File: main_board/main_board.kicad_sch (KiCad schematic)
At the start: 4 parts

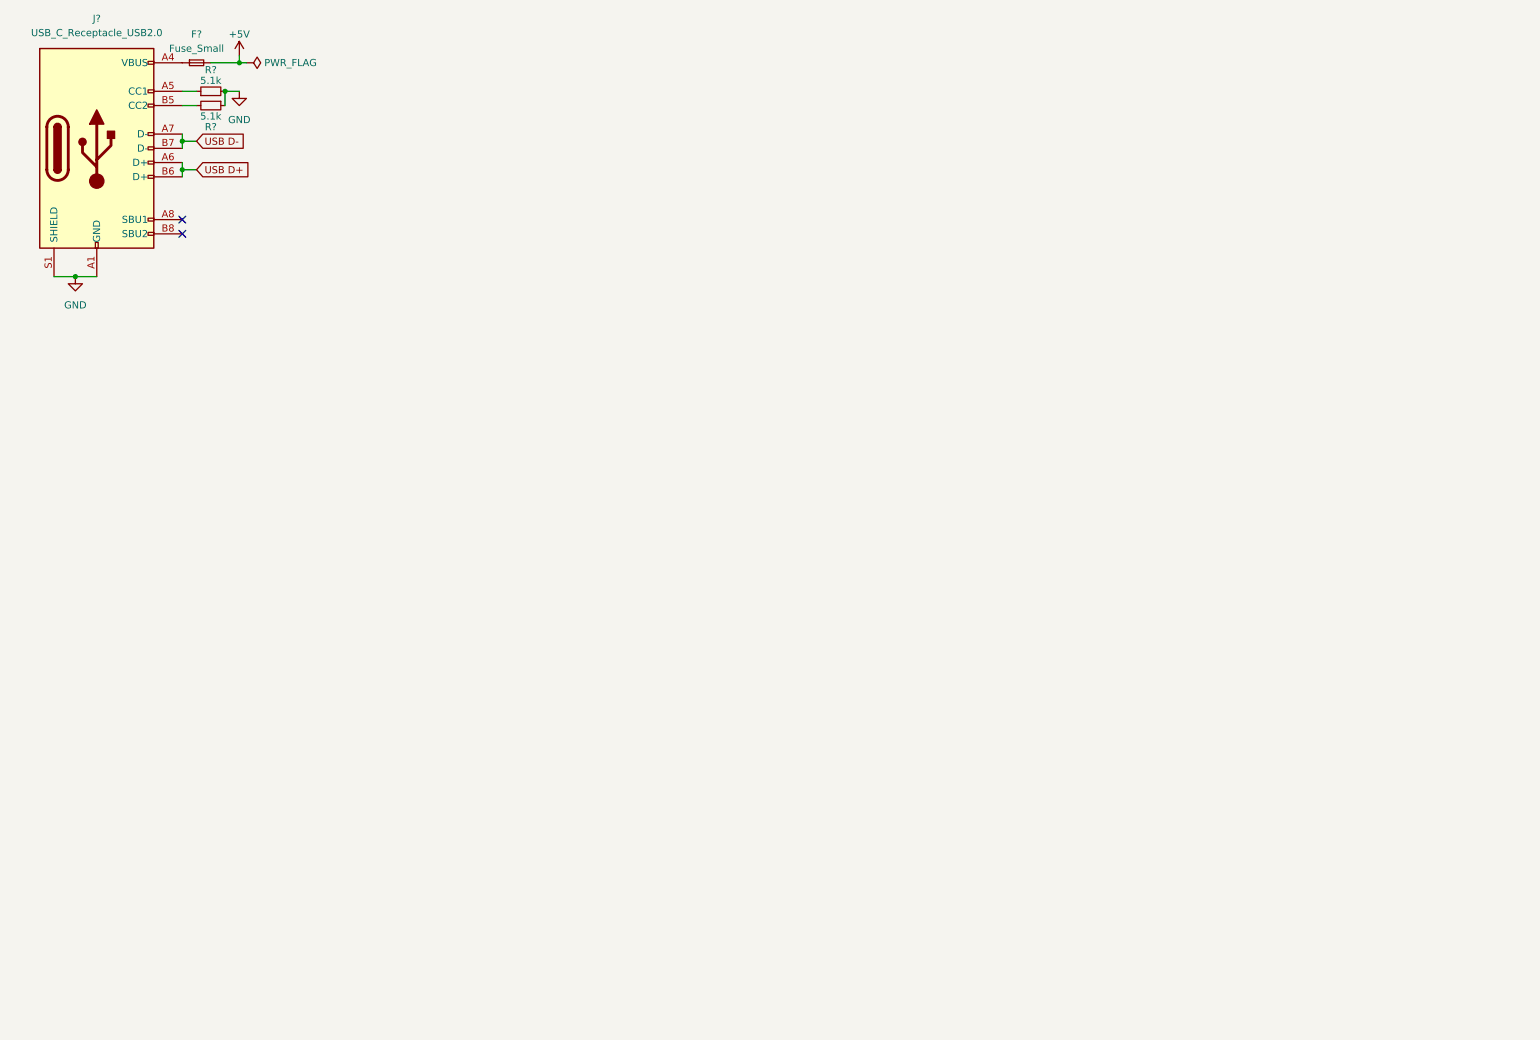
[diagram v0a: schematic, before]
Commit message: Main board schematic updates
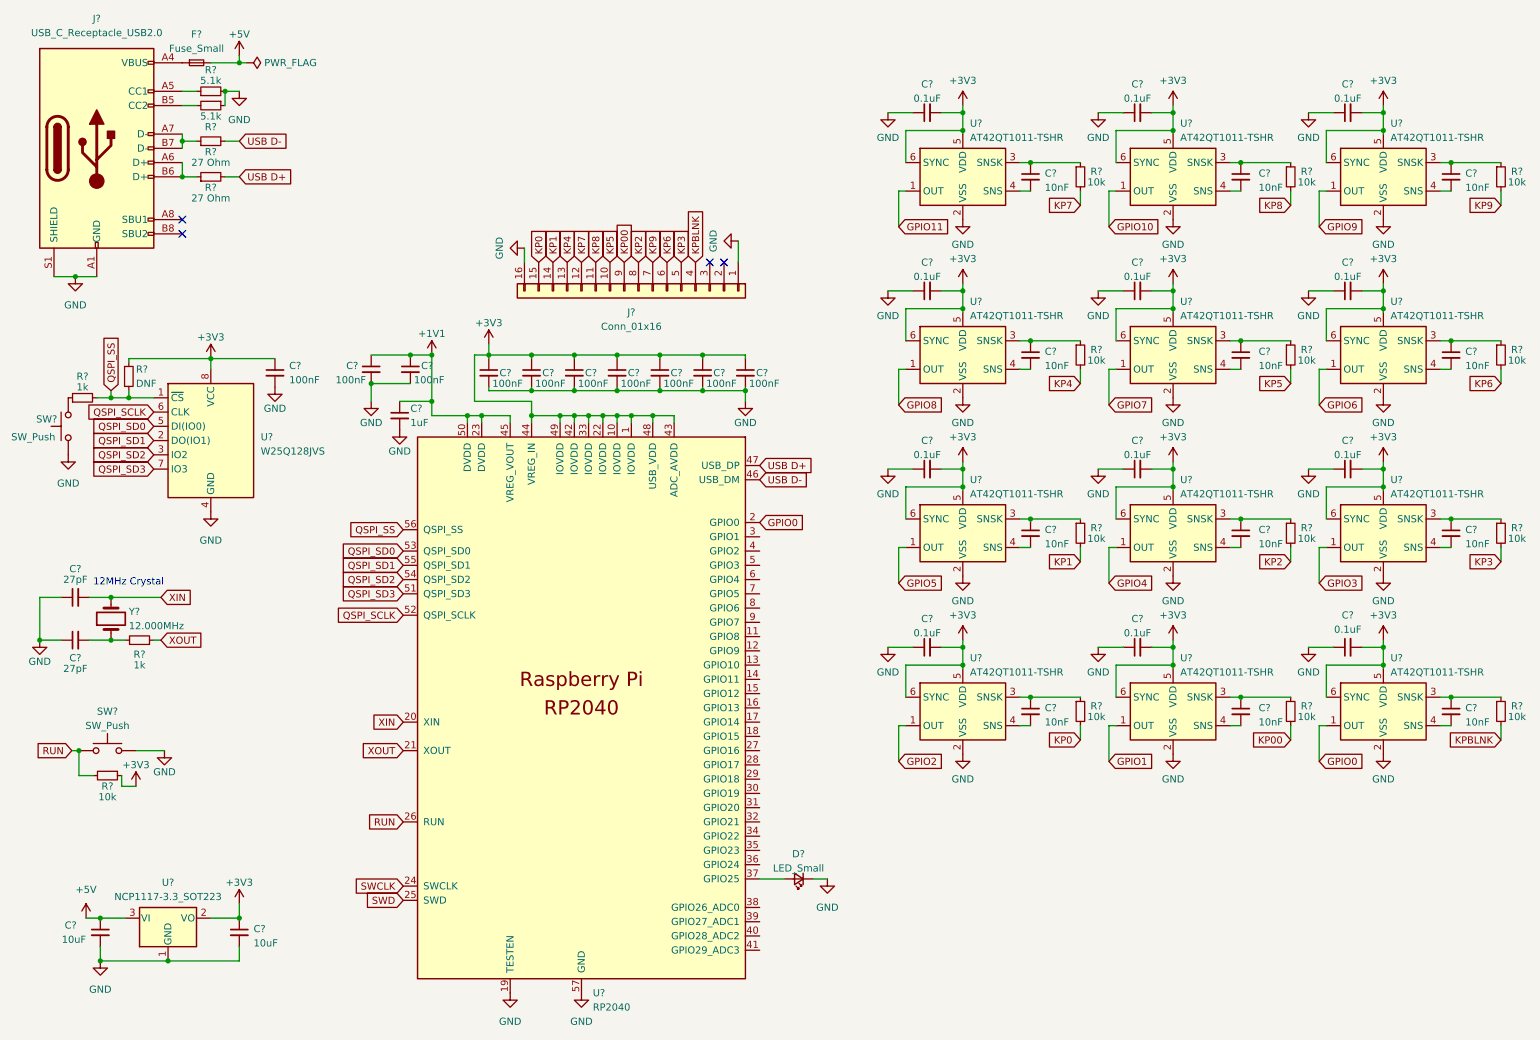
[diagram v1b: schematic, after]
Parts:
- added C? (x12): 0.1uF, symbol Device:C_Small
- added C? (x9): 100nF, symbol Device:C_Small
- added C? (x12): 10nF, symbol Device:C_Small
- added C?: 1uF, symbol Device:C_Small
- added C? (x2): 27pF, Capacitor_SMD:C_0402_1005Metric_Pad0.74x0.62mm_HandSolder, symbol Device:C_Small
- added C?: 100nF, Capacitor_SMD:C_0402_1005Metric_Pad0.74x0.62mm_HandSolder, symbol Device:C_Small
- added C? (x2): 10uF, Capacitor_SMD:C_0402_1005Metric_Pad0.74x0.62mm_HandSolder, symbol Device:C_Small
- added D?: LED_Small, LED_SMD:LED_0805_2012Metric_Pad1.15x1.40mm_HandSolder, symbol Device:LED_Small
- added J?: Conn_01x16, symbol Connector_Generic:Conn_01x16
- added R?: DNF, Resistor_SMD:R_0402_1005Metric_Pad0.72x0.64mm_HandSolder, symbol Device:R_Small
- added R? (x12): 10k, symbol Device:R_Small
- added R? (x2): 27 Ohm, symbol Device:R_Small
- added R? (x2): 1k, Resistor_SMD:R_0402_1005Metric_Pad0.72x0.64mm_HandSolder, symbol Device:R_Small
- added R?: 10k, Resistor_SMD:R_0402_1005Metric_Pad0.72x0.64mm_HandSolder, symbol Device:R_Small
- added SW?: SW_Push, Button_Switch_THT:SW_PUSH_6mm, symbol Switch:SW_Push
- added SW?: SW_Push, symbol Switch:SW_Push
- added U? (x12): AT42QT1011-TSHR, Package_TO_SOT_SMD:SOT-23-6, symbol Sensor_Touch:AT42QT1011-TSHR
- added U?: RP2040, RP2040_minimal:RP2040-QFN-56, symbol MCU_RaspberryPi_RP2040:RP2040
- added U?: W25Q128JVS, Package_SO:SOIC-8_5.23x5.23mm_P1.27mm, symbol Memory_Flash:W25Q128JVS
- added U?: NCP1117-3.3_SOT223, Package_TO_SOT_SMD:SOT-223-3_TabPin2, symbol Regulator_Linear:NCP1117-3.3_SOT223
- added Y?: 12.000MHz, Crystal:Crystal_HC49-4H_Vertical, symbol Device:Crystal
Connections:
- net +5V: now also C?.1, U?.3 (VI)
- net GND: now also C?.1, C?.1, C?.1, C?.1, C?.1, C?.1, C?.1, C?.1, C?.1, C?.1, C?.1, C?.1, C?.1, C?.1, C?.2, C?.2, C?.2, C?.2, C?.2, C?.2, C?.2, C?.2, C?.2, C?.2, C?.2, C?.2, C?.2, D?.1 (K), J?.1 (Pin_1), J?.16 (Pin_16), SW?.1, SW?.2, U?.1 (GND), U?.19 (TESTEN), U?.2 (VSS), U?.2 (VSS), U?.2 (VSS), U?.2 (VSS), U?.2 (VSS), U?.2 (VSS), U?.2 (VSS), U?.2 (VSS), U?.2 (VSS), U?.2 (VSS), U?.2 (VSS), U?.2 (VSS), U?.4 (GND), U?.57 (GND)
- net USB D+: now also R?.2, U?.47 (USB_DP); no longer J?.A6 (D+), J?.B6 (D+)
- net USB D-: now also R?.2, U?.46 (USB_DM); no longer J?.A7 (D-), J?.B7 (D-)
- new net: C?.1, R?.1, U?.3 (SNSK) (x12)
- new net: C?.2, U?.4 (SNS) (x12)
- new net: J?.A7 (D-), J?.B7 (D-), R?.1
- new net: D?.2 (A), U?.37 (GPIO25)
- new net: J?.A6 (D+), J?.B6 (D+), R?.1
- new net: C?.2, R?.1, Y?.1
- new net: R?.1, SW?.2
- new net +1V1: C?.1, C?.1, C?.1, U?.23 (DVDD), U?.45 (VREG_VOUT), U?.50 (DVDD)
- new net +3V3: C?.1, C?.1, C?.1, C?.1, C?.1, C?.1, C?.1, C?.1, C?.1, C?.2, C?.2, C?.2, C?.2, C?.2, C?.2, C?.2, C?.2, C?.2, C?.2, C?.2, C?.2, R?.1, R?.1, U?.1 (IOVDD), U?.10 (IOVDD), U?.2 (VO), U?.22 (IOVDD), U?.33 (IOVDD), U?.42 (IOVDD), U?.43 (ADC_AVDD), U?.44 (VREG_IN), U?.48 (USB_VDD), U?.49 (IOVDD), U?.5 (VDD), U?.5 (VDD), U?.5 (VDD), U?.5 (VDD), U?.5 (VDD), U?.5 (VDD), U?.5 (VDD), U?.5 (VDD), U?.5 (VDD), U?.5 (VDD), U?.5 (VDD), U?.5 (VDD), U?.6 (SYNC), U?.6 (SYNC), U?.6 (SYNC), U?.6 (SYNC), U?.6 (SYNC), U?.6 (SYNC), U?.6 (SYNC), U?.6 (SYNC), U?.6 (SYNC), U?.6 (SYNC), U?.6 (SYNC), U?.6 (SYNC), U?.8 (VCC)
- new net GPIO0: U?.1 (OUT), U?.2 (GPIO0)
- new net GPIO1: U?.1 (OUT)
- new net GPIO10: U?.1 (OUT)
- new net GPIO11: U?.1 (OUT)
- new net GPIO2: U?.1 (OUT)
- new net GPIO3: U?.1 (OUT)
- new net GPIO4: U?.1 (OUT)
- new net GPIO5: U?.1 (OUT)
- new net GPIO6: U?.1 (OUT)
- new net GPIO7: U?.1 (OUT)
- new net GPIO8: U?.1 (OUT)
- new net GPIO9: U?.1 (OUT)
- new net KP0: J?.15 (Pin_15), R?.2
- new net KP00: J?.9 (Pin_9), R?.2
- new net KP1: J?.14 (Pin_14), R?.2
- new net KP2: J?.8 (Pin_8), R?.2
- new net KP3: J?.5 (Pin_5), R?.2
- new net KP4: J?.13 (Pin_13), R?.2
- new net KP5: J?.10 (Pin_10), R?.2
- new net KP6: J?.6 (Pin_6), R?.2
- new net KP7: J?.12 (Pin_12), R?.2
- new net KP8: J?.11 (Pin_11), R?.2
- new net KP9: J?.7 (Pin_7), R?.2
- new net KPBLNK: J?.4 (Pin_4), R?.2
- new net QSPI_SCLK: U?.52 (QSPI_SCLK), U?.6 (CLK)
- new net QSPI_SD0: U?.5 (DI(IO0)), U?.53 (QSPI_SD0)
- new net QSPI_SD1: U?.2 (DO(IO1)), U?.55 (QSPI_SD1)
- new net QSPI_SD2: U?.3 (IO2), U?.54 (QSPI_SD2)
- new net QSPI_SD3: U?.51 (QSPI_SD3), U?.7 (IO3)
- new net QSPI_SS: R?.2, R?.2, U?.1 (~{CS}), U?.56 (QSPI_SS)
- new net RUN: R?.2, SW?.1, U?.26 (RUN)
- new net SWCLK: U?.24 (SWCLK)
- new net SWD: U?.25 (SWD)
- new net XIN: C?.2, U?.20 (XIN), Y?.2
- new net XOUT: R?.2, U?.21 (XOUT)
- no-connect marks 2 -> 4
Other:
- note added: "12MHz Crystal"

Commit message: done RP2040 routing, near final component layout
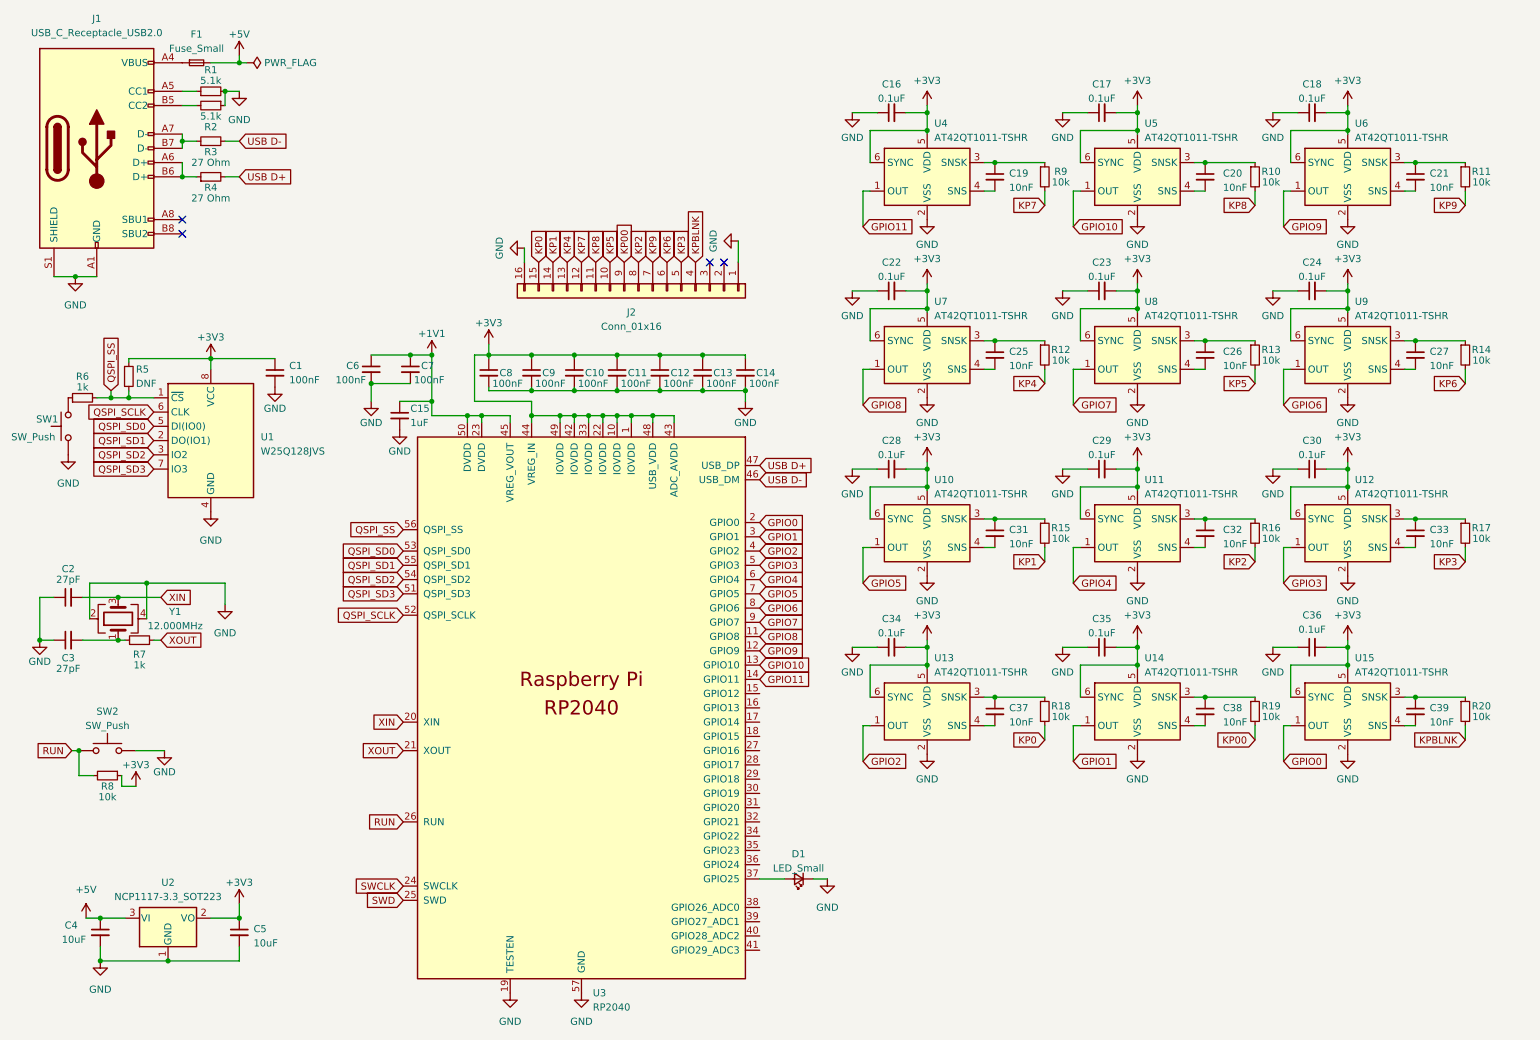
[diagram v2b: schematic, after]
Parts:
- removed Y?: 12.000MHz, Crystal:Crystal_HC49-4H_Vertical, symbol Device:Crystal
- added Y1: 12.000MHz, Crystal:Crystal_SMD_3225-4Pin_3.2x2.5mm_HandSoldering, symbol Device:Crystal_GND24
- C10, C11, C12, C13, C14, C15, C16, C17, C18, C19, C20, C21, C22, C23, C24, C25, C26, C27, C28, C29, C30, C31, C32, C33, C34, C35, C36, C37, C38, C39, C6, C7, C8, C9: renamed from C?; footprint (none) -> Capacitor_SMD:C_0603_1608Metric_Pad1.08x0.95mm_HandSolder
- F1: renamed from F?; footprint (none) -> Fuse:Fuse_1206_3216Metric_Pad1.42x1.75mm_HandSolder
- J1: renamed from J?; footprint (none) -> Connector_USB:USB_C_Receptacle_JAE_DX07S016JA1R1500
- J2: renamed from J?; footprint (none) -> Connector_FFC-FPC:TE_1-84952-6_1x16-1MP_P1.0mm_Horizontal
- R1, R10, R11, R12, R13, R14, R15, R16, R17, R18, R19, R2, R20, R3, R4, R9: renamed from R?; footprint (none) -> Resistor_SMD:R_0603_1608Metric_Pad0.98x0.95mm_HandSolder
- SW1: renamed from SW?; footprint (none) -> Button_Switch_THT:SW_PUSH_6mm
- gave numbers to parts that had none: 26
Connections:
- net GND: now also Y1.2, Y1.4
- net GPIO1: now also U3.3 (GPIO1)
- net GPIO10: now also U3.13 (GPIO10)
- net GPIO11: now also U3.14 (GPIO11)
- net GPIO2: now also U3.4 (GPIO2)
- net GPIO3: now also U3.5 (GPIO3)
- net GPIO4: now also U3.6 (GPIO4)
- net GPIO5: now also U3.7 (GPIO5)
- net GPIO6: now also U3.8 (GPIO6)
- net GPIO7: now also U3.9 (GPIO7)
- net GPIO8: now also U3.11 (GPIO8)
- net GPIO9: now also U3.12 (GPIO9)
- net XIN: now also Y1.3
- net at C3.2, R7.1: now also Y1.1
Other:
- note removed: "12MHz Crystal"
- moved on the sheet: C16, C17, C18, C19, C2, C20, C21, C22, C23, C24, C25, C26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

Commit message: move to MPR121
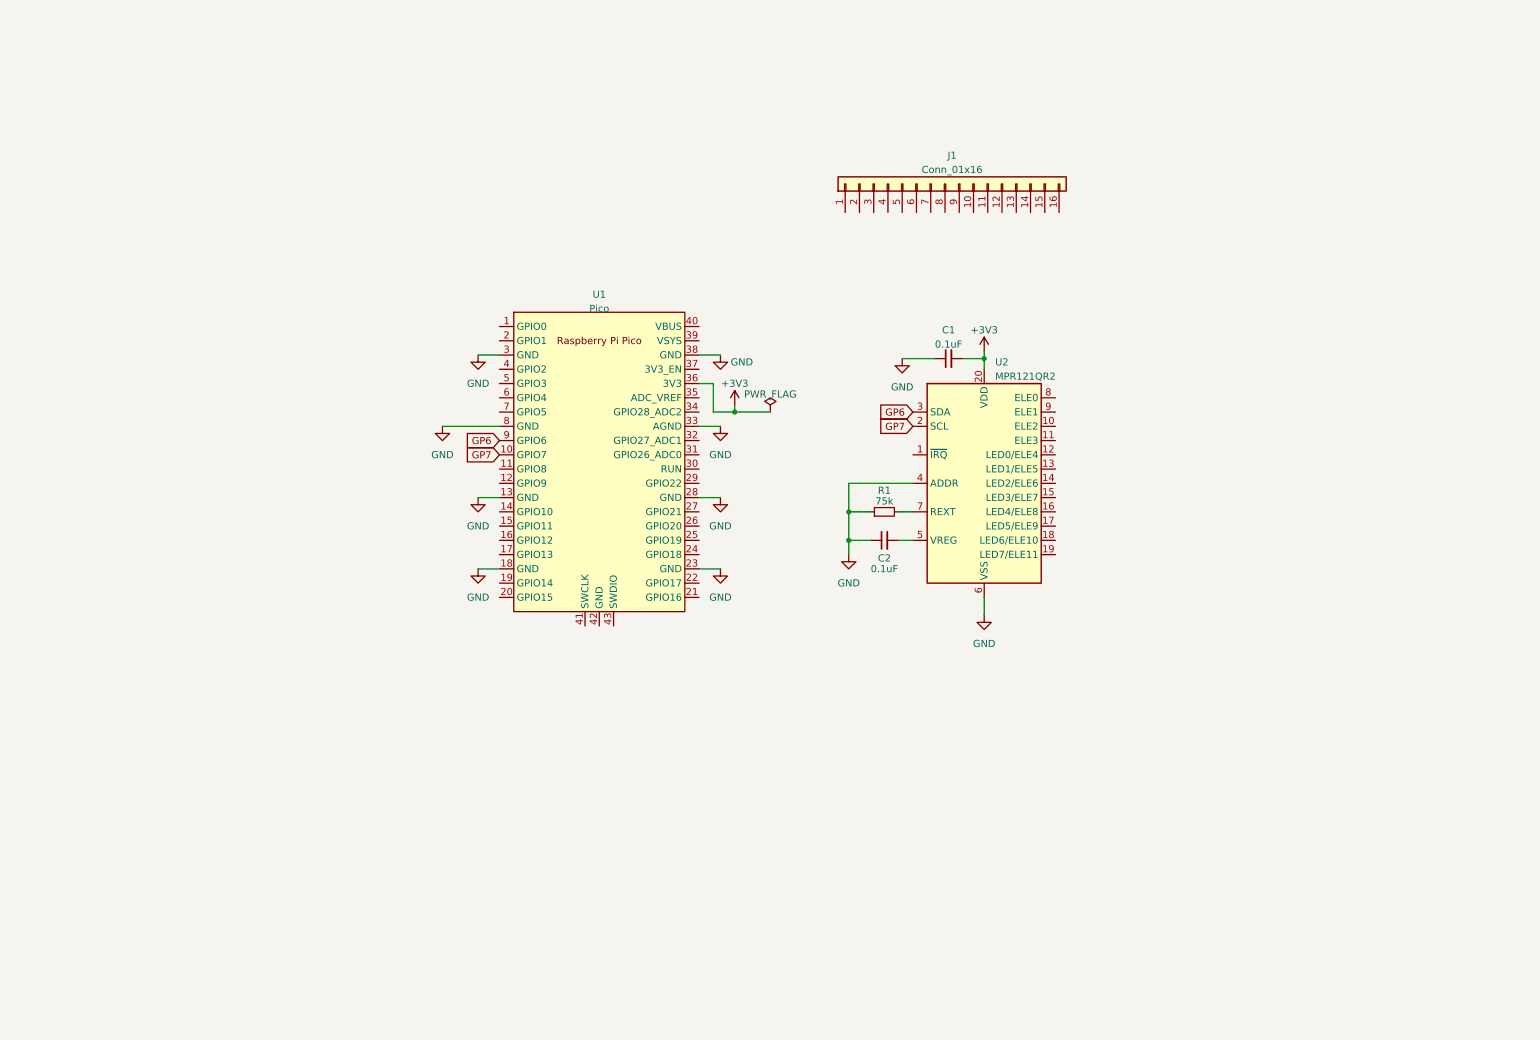
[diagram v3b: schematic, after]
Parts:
- removed C10, C11, C12, C13, C14, C6, C7, C8, C9: 100nF, Capacitor_SMD:C_0603_1608Metric_Pad1.08x0.95mm_HandSolder, symbol Device:C_Small
- removed C15: 1uF, Capacitor_SMD:C_0603_1608Metric_Pad1.08x0.95mm_HandSolder, symbol Device:C_Small
- removed C16, C17, C18, C22, C23, C24, C28, C29, C30, C34, C35, C36: 0.1uF, Capacitor_SMD:C_0603_1608Metric_Pad1.08x0.95mm_HandSolder, symbol Device:C_Small
- removed C19, C20, C21, C25, C26, C27, C31, C32, C33, C37, C38, C39: 10nF, Capacitor_SMD:C_0603_1608Metric_Pad1.08x0.95mm_HandSolder, symbol Device:C_Small
- removed C3: 27pF, Capacitor_SMD:C_0402_1005Metric_Pad0.74x0.62mm_HandSolder, symbol Device:C_Small
- removed C4, C5: 10uF, Capacitor_SMD:C_0402_1005Metric_Pad0.74x0.62mm_HandSolder, symbol Device:C_Small
- removed D1: LED_Small, LED_SMD:LED_0805_2012Metric_Pad1.15x1.40mm_HandSolder, symbol Device:LED_Small
- removed F1: Fuse_Small, Fuse:Fuse_1206_3216Metric_Pad1.42x1.75mm_HandSolder, symbol Device:Fuse_Small
- removed J1: USB_C_Receptacle_USB2.0, Connector_USB:USB_C_Receptacle_JAE_DX07S016JA1R1500, symbol Connector:USB_C_Receptacle_USB2.0
- removed J2: Conn_01x16, Connector_FFC-FPC:TE_1-84952-6_1x16-1MP_P1.0mm_Horizontal, symbol Connector_Generic:Conn_01x16
- removed R10, R11, R12, R13, R14, R15, R16, R17, R18, R19, R20, R9: 10k, Resistor_SMD:R_0603_1608Metric_Pad0.98x0.95mm_HandSolder, symbol Device:R_Small
- removed R2: 5.1k, Resistor_SMD:R_0603_1608Metric_Pad0.98x0.95mm_HandSolder, symbol Device:R_Small
- removed R3, R4: 27 Ohm, Resistor_SMD:R_0603_1608Metric_Pad0.98x0.95mm_HandSolder, symbol Device:R_Small
- removed R5: DNF, Resistor_SMD:R_0402_1005Metric_Pad0.72x0.64mm_HandSolder, symbol Device:R_Small
- removed R6, R7: 1k, Resistor_SMD:R_0402_1005Metric_Pad0.72x0.64mm_HandSolder, symbol Device:R_Small
- removed R8: 10k, Resistor_SMD:R_0402_1005Metric_Pad0.72x0.64mm_HandSolder, symbol Device:R_Small
- removed SW1, SW2: SW_Push, Button_Switch_THT:SW_PUSH_6mm, symbol Switch:SW_Push
- removed U1: W25Q128JVS, Package_SO:SOIC-8_5.23x5.23mm_P1.27mm, symbol Memory_Flash:W25Q128JVS
- removed U10, U11, U12, U13, U14, U15, U4, U5, U6, U7, U8, U9: AT42QT1011-TSHR, Package_TO_SOT_SMD:SOT-23-6, symbol Sensor_Touch:AT42QT1011-TSHR
- removed U2: NCP1117-3.3_SOT223, Package_TO_SOT_SMD:SOT-223-3_TabPin2, symbol Regulator_Linear:NCP1117-3.3_SOT223
- removed U3: RP2040, RP2040_minimal:RP2040-QFN-56, symbol MCU_RaspberryPi_RP2040:RP2040
- removed Y1: 12.000MHz, Crystal:Crystal_SMD_3225-4Pin_3.2x2.5mm_HandSoldering, symbol Device:Crystal_GND24
- added J1: Conn_01x16, symbol Connector_Generic:Conn_01x16
- added U1: Pico, RPi_Pico:RPi_Pico_SMD_TH, symbol MCU_RaspberryPi_and_Boards:Pico
- added U2: MPR121QR2, Package_DFN_QFN:UQFN-20_3x3mm_P0.4mm, symbol Sensor_Touch:MPR121QR2
- C1: value 100nF -> 0.1uF; footprint Capacitor_SMD:C_0402_1005Metric_Pad0.74x0.62mm_HandSolder -> (none); LCSC C1525 -> (none)
- C2: value 27pF -> 0.1uF; footprint Capacitor_SMD:C_0402_1005Metric_Pad0.74x0.62mm_HandSolder -> (none); LCSC C1557 -> (none)
- R1: value 5.1k -> 75k; footprint Resistor_SMD:R_0603_1608Metric_Pad0.98x0.95mm_HandSolder -> (none)
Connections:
- net +3V3: now also C1.2, U1.36 (3V3), U2.20 (VDD); no longer C1.1
- net GND: now also C1.1, R1.1, U1.13 (GND), U1.18 (GND), U1.23 (GND), U1.28 (GND), U1.3 (GND), U1.33 (AGND), U1.38 (GND), U1.8 (GND), U2.4 (ADDR), U2.6 (VSS); no longer C1.2, R1.2
- net XIN: no longer names the net of C2.2
- net XIN: now also U2.5 (VREG)
- new net: R1.2, U2.7 (REXT)
- new net GP6: U1.9 (GPIO6), U2.3 (SDA)
- new net GP7: U1.10 (GPIO7), U2.2 (SCL)
- no-connect marks 4 -> 0
